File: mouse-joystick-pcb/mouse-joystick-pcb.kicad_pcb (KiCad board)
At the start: 4 copper layers, 60 x 160 mm, 77 parts, among them J1001 FFC_P1mm_BOT_RA_SMD, J1101 FFC_P1mm_BOT_RA_SMD, J501 FFC_P1mm_BOT_RA_SMD, J601 FFC_P1mm_BOT_RA_SMD, J701 FFC_P1mm_BOT_RA_SMD, J801 FFC_P1mm_BOT_RA_SMD, J901 FFC_P1mm_BOT_RA_SMD, Q301 MOSFET-N-CH-EN_100V_260mA, Q302 MOSFET-P-CH-EN_60V_50A, T301 TERM_BLK_HDR_2POS_90DEG_0.2IN, U1001 MAX13431E, U1101 MAX13431E, U301 TPSM365R6V5RDNR, U501 MAX13431E, U601 MAX13431E, U701 MAX13431E, U801 MAX13431E, U901 MAX13431E

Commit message: Adjust schmatic
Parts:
- removed A401: PICO_W5500_EVB, Janelia:Pico-W5500-EVB_Header_Holes
- removed C1001, C1101, C302, C501, C601, C701, C801, C901: 0.1uF_100V, Janelia:C_0402_1005Metric
- removed C1002, C1102, C502, C602, C702, C802, C902: 1uF_35V, Janelia:C_0402_1005Metric
- removed C301: 3.3uF_50V, Janelia:C_1210_3225Metric
- removed C303, C304: 1uF_25V, Janelia:C_0402_1005Metric
- removed D1001, D1101, D501, D601, D701, D801, D901: D_Zener_47V_1W, Janelia:D_SMA
- removed D1002, D1102, D502, D602, D702, D802, D902: D, Janelia:D_SMB
- removed D301: D_50V_15A, Janelia:POWERDI5_DIO
- removed D401: D_SCHOTTKY_20V_1A, Janelia:DIOM3616X98N
- removed FID201, FID202, FID203, FID204: FIDUCIAL_0.5mm_MASK1mm, Janelia:FIDUCIAL_0.5mm_Mask1mm
- removed H201, H202, H203, H204: MountingHole_M3_Pad, Janelia:MountingHole_3.2mm_M3_Pad
- removed J1001, J1101, J501, J601, J701, J801, J901: FFC_P1mm_BOT_RA_SMD, Janelia:CONN_C2914097
- removed Q301: MOSFET-N-CH-EN_100V_260mA, Janelia:SOT-23
- removed Q302: MOSFET-P-CH-EN_60V_50A, Janelia:TO-252-2
- removed R1001, R1101, R501, R601, R701, R801, R901: 0.24, Janelia:R_2512_6332Metric
- removed R1002, R1102, R502, R602, R702, R802, R902: 100, Janelia:R_0402_1005Metric
- removed R301: 1k, Janelia:R_0402_1005Metric
- removed R302: 3.6k, Janelia:R_0402_1005Metric
- removed T301: TERM_BLK_HDR_2POS_90DEG_0.2IN, Janelia:PHOENIX_1757242
- removed U1001, U1101, U501, U601, U701, U801, U901: MAX13431E, Janelia:21-0137I_T1033-1_MXM
- removed U301: TPSM365R6V5RDNR, Janelia:RDN0011A-MFG
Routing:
- net /GND: track 631.7 -> 0.00 mm, vias 31 -> 0
- net /+5V: track 263.8 -> 0.00 mm, vias 9 -> 0
- net /+3.3V: track 186.5 -> 0.00 mm, vias 7 -> 0
- net /VCC: track 160.5 -> 0.00 mm
- net /RX: track 150.3 -> 0.00 mm, vias 7 -> 0
- net /TX: track 147.8 -> 0.00 mm, vias 7 -> 0
- net /ENABLE_TX_6: track 77.9 -> 0.00 mm, vias 1 -> 0
- net /~{ENABLE_RX_6}: track 76.8 -> 0.00 mm, vias 1 -> 0
- net /power/VBB: track 66.0 -> 0.00 mm
- net /ENABLE_TX_5: track 62.2 -> 0.00 mm, vias 1 -> 0
- net /~{ENABLE_RX_5}: track 61.3 -> 0.00 mm, vias 1 -> 0
- net /ENABLE_TX_4: track 55.1 -> 0.00 mm, vias 1 -> 0
- net /power/~{ENABLE_VCC}: track 55.0 -> 0.00 mm, vias 2 -> 0
- net /~{ENABLE_RX_4}: track 54.5 -> 0.00 mm, vias 1 -> 0
- net /ENABLE_TX_3: track 38.4 -> 0.00 mm, vias 1 -> 0
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- removed copper zone on B.Cu, net /GND
- removed copper zone on In1.Cu, net /GND
- removed copper zone on In2.Cu, net /GND
- removed copper zone on F.Cu, net /VCC
- removed copper zone on F.Cu, net /power/VAA
- removed copper zone on F.Cu, net /power/VBB

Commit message: Initial pcb import
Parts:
- added A401: TEENSY_4.0_HEADERS, Janelia:TEENSY_4.0_HEADERS, F.Cu at (92.4, 39.7)
- added C301: 3.3uF_50V, Janelia:C_1210_3225Metric, F.Cu at (157.4, 39.2)
- added C302: 0.1uF_100V, Janelia:C_0402_1005Metric, F.Cu at (153.1, 38.1)
- added C303: 1uF_25V, Janelia:C_0402_1005Metric, F.Cu at (153.1, 40.1)
- added C304: 1uF_25V, Janelia:C_0402_1005Metric, F.Cu at (153.1, 42.0)
- added C305: 47uF_10V, Janelia:C_0805_2012Metric, F.Cu at (162.4, 38.6)
- added C501: 0.1uF_100V, Janelia:C_0402_1005Metric, F.Cu at (-57.2, 40.2)
- added C502: 0.1uF_100V, Janelia:C_0402_1005Metric, F.Cu at (-57.2, 42.1)
- added C503: 22nF_100V, Janelia:C_0603_1608Metric, F.Cu at (-86.0, 60.1)
- added C504: 0.1uF_100V, Janelia:C_0402_1005Metric, F.Cu at (-57.2, 44.1)
- added C505: 0.1uF_100V, Janelia:C_0402_1005Metric, F.Cu at (-57.2, 46.1)
- added C506: 0.47uF_35V, Janelia:C_0402_1005Metric, F.Cu at (-57.2, 48.0)
- added C507: 47uF_10V, Janelia:C_0805_2012Metric, F.Cu at (-54.7, 28.5)
- added C508: 0.1uF_100V, Janelia:C_0402_1005Metric, F.Cu at (-54.3, 40.2)
- added C509: 0.1uF_100V, Janelia:C_0402_1005Metric, F.Cu at (-54.3, 42.1)
- added C510: 0.1uF_100V, Janelia:C_0402_1005Metric, F.Cu at (-54.3, 44.1)
- added C511: 0.1uF_100V, Janelia:C_0402_1005Metric, F.Cu at (-54.3, 46.1)
- added C512: 2.2uF_100V, Janelia:C_0805_2012Metric, F.Cu at (-54.7, 31.5)
- added C513: 2.2uF_100V, Janelia:C_0805_2012Metric, F.Cu at (-54.7, 34.5)
- added C514: 100uF_50V, Janelia:CAP_EEEHAH101UAP, F.Cu at (-81.7, 44.1)
- added C515: 100uF_50V, Janelia:CAP_EEEHAH101UAP, F.Cu at (-81.7, 54.0)
- added C516: 0.1uF_100V, Janelia:C_0402_1005Metric, F.Cu at (-54.3, 48.0)
- added C517: 2.2uF_100V, Janelia:C_0805_2012Metric, F.Cu at (-54.7, 37.5)
- added C601: 0.22uF_25V, Janelia:C_0402_1005Metric, F.Cu at (-50.4, 88.5)
- added C602: 0.22uF_25V, Janelia:C_0402_1005Metric, F.Cu at (-50.4, 90.5)
- added C603: 1uF_35V, Janelia:C_0402_1005Metric, F.Cu at (-50.4, 92.5)
- added C604: 0.22uF_25V, Janelia:C_0402_1005Metric, F.Cu at (-50.4, 94.4)
- added C701: 0.1uF_100V, Janelia:C_0402_1005Metric, F.Cu at (-36.4, 39.6)
- added C702: 0.1uF_100V, Janelia:C_0402_1005Metric, F.Cu at (-36.4, 41.6)
- added C703: 22nF_100V, Janelia:C_0603_1608Metric, F.Cu at (-22.4, 55.6)
- added C704: 0.1uF_100V, Janelia:C_0402_1005Metric, F.Cu at (-36.4, 43.5)
- added C705: 0.1uF_100V, Janelia:C_0402_1005Metric, F.Cu at (-36.4, 45.5)
- added C706: 0.47uF_35V, Janelia:C_0402_1005Metric, F.Cu at (-36.4, 47.5)
- added C707: 47uF_10V, Janelia:C_0805_2012Metric, F.Cu at (-22.6, 40.1)
- added C708: 0.1uF_100V, Janelia:C_0402_1005Metric, F.Cu at (-36.4, 49.4)
- added C709: 0.1uF_100V, Janelia:C_0402_1005Metric, F.Cu at (-36.4, 51.4)
- added C710: 2.2uF_100V, Janelia:C_0805_2012Metric, F.Cu at (-22.6, 43.1)
- added C711: 2.2uF_100V, Janelia:C_0805_2012Metric, F.Cu at (-22.6, 46.1)
- added C712: 100uF_50V, Janelia:CAP_EEEHAH101UAP, F.Cu at (-44.1, 31.9)
- added C713: 100uF_50V, Janelia:CAP_EEEHAH101UAP, F.Cu at (-44.1, 41.8)
- added C801: 100uF_50V, Janelia:CAP_EEEHAH101UAP, F.Cu at (-23.3, 69.1)
- added D301: D_50V_15A, Janelia:POWERDI5_DIO, F.Cu at (112.4, 44.1)
- added D302: LED_RED, Janelia:LED_0402-1005_KNB, F.Cu at (142.4, 24.1)
- added FID201: FIDUCIAL_0.5mm_MASK1mm, Janelia:FIDUCIAL_0.5mm_Mask1mm, F.Cu at (74.9, 31.6)
- added FID202: FIDUCIAL_0.5mm_MASK1mm, Janelia:FIDUCIAL_0.5mm_Mask1mm, F.Cu at (129.9, 31.6)
- added FID203: FIDUCIAL_0.5mm_MASK1mm, Janelia:FIDUCIAL_0.5mm_Mask1mm, F.Cu at (129.9, 171.6)
- added FID204: FIDUCIAL_0.5mm_MASK1mm, Janelia:FIDUCIAL_0.5mm_Mask1mm, F.Cu at (74.9, 171.6)
- added H201: MountingHole_M3_Pad, Janelia:MountingHole_3.2mm_M3_Pad, F.Cu at (77.4, 26.6)
- added H202: MountingHole_M3_Pad, Janelia:MountingHole_3.2mm_M3_Pad, F.Cu at (127.4, 26.6)
- added H203: MountingHole_M3_Pad, Janelia:MountingHole_3.2mm_M3_Pad, F.Cu at (127.4, 176.6)
- added H204: MountingHole_M3_Pad, Janelia:MountingHole_3.2mm_M3_Pad, F.Cu at (77.4, 176.6)
- added J301: 2.1, Janelia:Connector_BarrelJack_XKB_2.1, F.Cu at (112.4, 29.1)
- added J501: Conn_01x02_P3.5mm_TBH_Horizontal_Screw, Janelia:PhoenixContact_MC_1,5_2-G-3.5_1x02_P3.50mm_Horizontal_Screw, F.Cu at (-61.9, 30.2)
- added J502: Conn_01x04_P3.5mm_TBH_Horizontal_Screw, Janelia:PhoenixContact_MC_1,5_4-G-3.5_1x04_P3.50mm_Horizontal_Screw, F.Cu at (-67.0, 42.2)
- added J503: Conn_01x05_P3.5mm_TBH_Horizontal_Screw, Janelia:PhoenixContact_MC_1,5_5-G-3.5_1x05_P3.50mm_Horizontal_Screw, F.Cu at (-77.4, 30.2)
- added J701: Conn_01x02_P3.5mm_TBH_Horizontal_Screw, Janelia:PhoenixContact_MC_1,5_2-G-3.5_1x02_P3.50mm_Horizontal_Screw, F.Cu at (-29.9, 41.8)
- added J702: Conn_01x04_P3.5mm_TBH_Horizontal_Screw, Janelia:PhoenixContact_MC_1,5_4-G-3.5_1x04_P3.50mm_Horizontal_Screw, F.Cu at (-29.4, 30.1)
- added J801: Conn_01x02_P3.5mm_TBH_Horizontal_Screw, Janelia:PhoenixContact_MC_1,5_2-G-3.5_1x02_P3.50mm_Horizontal_Screw, F.Cu at (-24.6, 77.1)
- added R301: 2.32k, Janelia:R_0805_2012Metric, F.Cu at (138.3, 27.7)
- added R501: 0.36, Janelia:R_1206_3216Metric, F.Cu at (-61.2, 52.4)
- added R502: 0.36, Janelia:R_1206_3216Metric, F.Cu at (-61.2, 55.7)
- added R503: 10, Janelia:R_0402_1005Metric, F.Cu at (-56.9, 58.8)
- added R504: 200k, Janelia:R_0402_1005Metric, F.Cu at (-56.9, 60.8)
- added R601: 40k, Janelia:R_0603_1608Metric, F.Cu at (-49.8, 96.7)
- added R602: 40k, Janelia:R_0603_1608Metric, F.Cu at (-49.8, 99.2)
- added R701: 0.12, Janelia:R_1206_3216Metric, F.Cu at (-32.1, 52.2)
- added R702: 0.12, Janelia:R_1206_3216Metric, F.Cu at (-32.1, 55.5)
- added R703: 10, Janelia:R_0402_1005Metric, F.Cu at (-27.9, 56.1)
- added R801: 30, Janelia:R_0402_1005Metric, F.Cu at (-18.1, 79.4)
- added SP601: Speaker_13x13mm_8Ohm_700mW, Janelia:Speaker_13x13mm_KLJ-01304T-08R07W, F.Cu at (-59.3, 94.8)
- added U301: TPSM365R6V5RDNR, Janelia:RDN0011A-MFG, F.Cu at (149.0, 40.5)
- added U501: MAX6816, Janelia:SOT192P237X122-4N, F.Cu at (-61.5, 59.7)
- added U502: TMC5130A-TA, Janelia:TQFP-48-1EP_7x7mm_P0.5mm_EP5x5mm_ThermalVias, F.Cu at (-69.7, 56.5)
- added U503: Logic_LevelTranslator_LSF0102DCUR, Janelia:SOP50P310X90-8N, F.Cu at (-55.1, 52.4)
- added U601: TPA6204A1DRBR, Janelia:DRB8_1P75X1P5, F.Cu at (-63.8, 104.4)
- added U701: MAX6816, Janelia:SOT192P237X122-4N, F.Cu at (-26.9, 52.8)
- added U702: TMC5130A-TA, Janelia:TQFP-48-1EP_7x7mm_P0.5mm_EP5x5mm_ThermalVias, F.Cu at (-44.8, 52.4)
- added U801: 40V_200mA, Janelia:SC-74-6_1.55x2.9mm_P0.95mm, F.Cu at (-16.2, 76.2)
- added X501: 16MHz_3.3V, Janelia:OSC_ECS-2520S33-160-FN-TR, F.Cu at (-55.8, 55.9)
- added X701: 16MHz_3.3V, Janelia:OSC_ECS-2520S33-160-FN-TR, F.Cu at (-21.8, 52.4)
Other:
- board text added: "+24VDC Center Positive"
- board text added: "mouse-joystick-pcb v1.0 2024/10"
- board text removed: "+48VDC"
- board text removed: "0"
- board text removed: "1"
- board text removed: "2"
- board text removed: "3"
- board text removed: "4"
- board text removed: "5"
- board text removed: "6"
- board text removed: "GND"
- board text removed: "RX"
- board text removed: "TX"
- board text removed: "mouse-joystick-pcb v1.0 2024/07"

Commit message: Initial footprint layout
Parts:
- moved J503 210.1 mm to (124.4, 88.6), turned to 90 degrees
- moved C503 200.6 mm to (114.4, 70.1)
- moved C712 194.4 mm to (116.4, 141.6), turned to -90 degrees
- moved J502 193.5 mm to (124.4, 70.6), turned to 90 degrees
- moved C515 193.4 mm to (108.4, 89.6), turned to 180 degrees
- moved C701 190.9 mm to (122.4, 145.6), turned to 180 degrees
- moved C514 190.9 mm to (108.4, 61.6), turned to 180 degrees
- moved J501 188.3 mm to (124.4, 57.6), turned to 90 degrees
- moved J701 183.4 mm to (115.4, 153.6)
- moved C517 181.3 mm to (120.4, 84.6), turned to 90 degrees
- moved J702 180.7 mm to (102.4, 153.6)
- moved U502 180.1 mm to (109.4, 75.6)
- moved U501 180.0 mm to (118.4, 57.6), turned to 180 degrees
- moved C516 179.4 mm to (120.4, 88.6), turned to -90 degrees
- moved C511 177.6 mm to (117.4, 91.6)
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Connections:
- A401 pad 10: unconnected-(A401-D10/CS/MQSR/PWM-Pad10) -> /BRAKE_PWM
- A401 pad 22: /BRAKE_PWM -> unconnected-(A401-D22/A8/CTX1/PWM-Pad22)
- A401 pad 23: /AUDIO -> unconnected-(A401-D23/A9/CRX1/MCLK1/PWM-Pad23)
- A401 pad 9: unconnected-(A401-D9/OUT1C/PWM-Pad9) -> /AUDIO
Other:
- board size 60 x 160 mm -> 60 x 120 mm

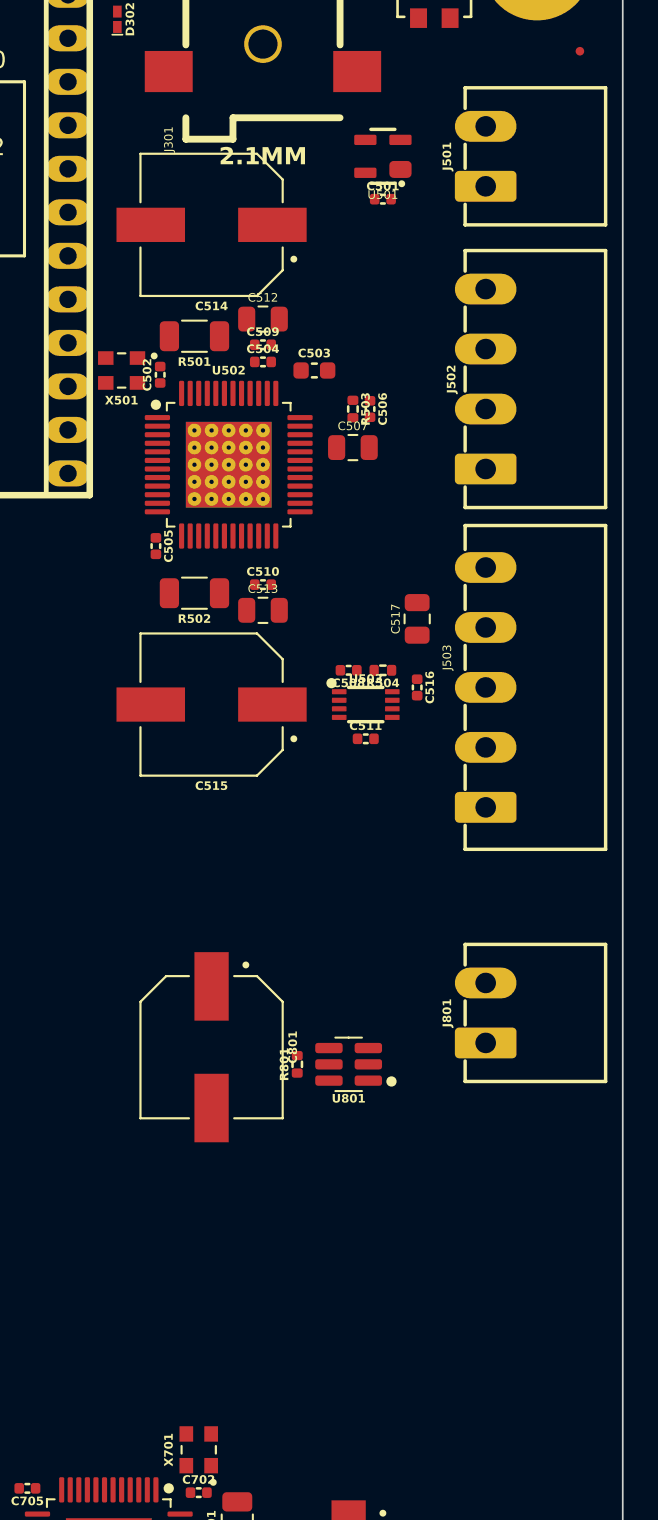
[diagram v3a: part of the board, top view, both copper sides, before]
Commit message: Add torque-sensor sheet
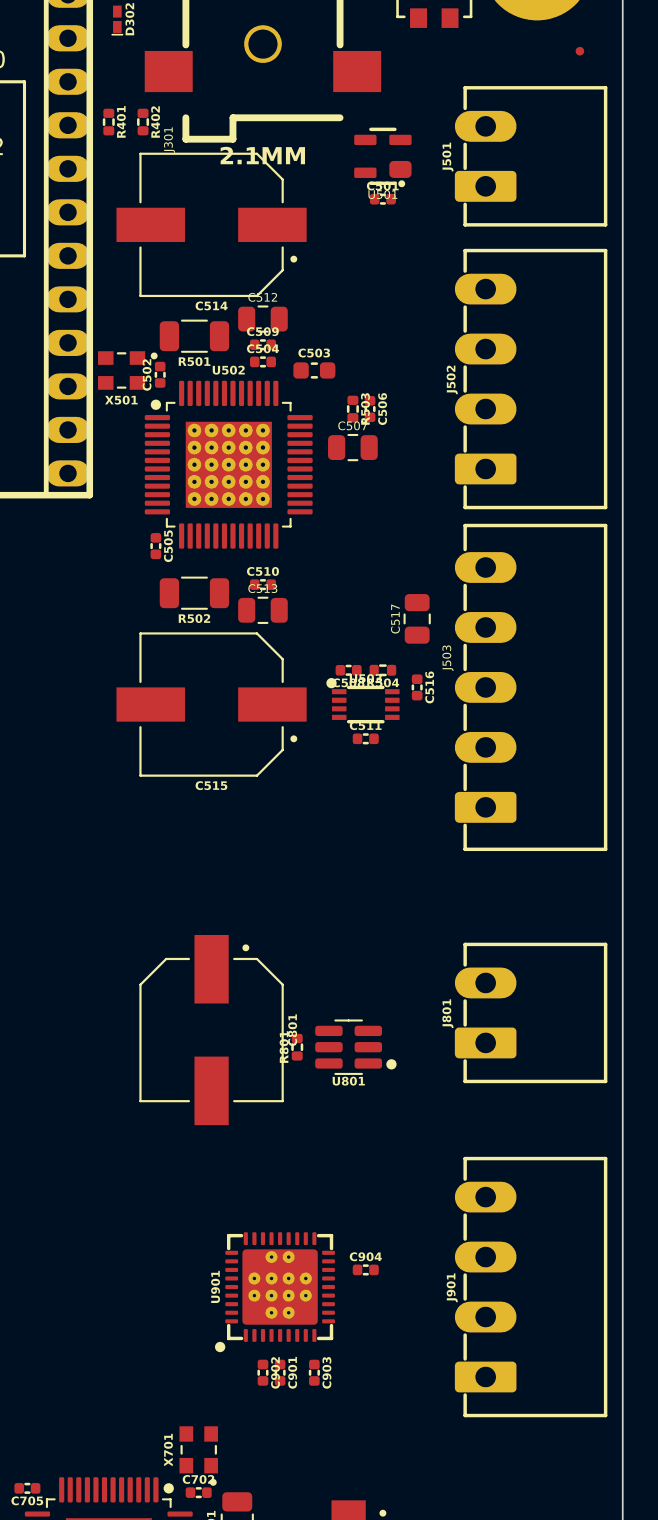
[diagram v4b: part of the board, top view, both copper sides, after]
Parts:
- added C901: 0.1uF_100V, Janelia:C_0402_1005Metric, F.Cu at (112.4, 128.6)
- added C902: 0.1uF_100V, Janelia:C_0402_1005Metric, F.Cu at (111.4, 128.6)
- added C903: 0.1uF_100V, Janelia:C_0402_1005Metric, F.Cu at (114.4, 128.6)
- added C904: 0.1uF_100V, Janelia:C_0402_1005Metric, F.Cu at (117.4, 122.6)
- added J901: Conn_01x04_P3.5mm_TBH_Horizontal_Screw, Janelia:PhoenixContact_MC_1,5_4-G-3.5_1x04_P3.50mm_Horizontal_Screw, F.Cu at (124.4, 123.6)
- added R401: 1.8k, Janelia:R_0402_1005Metric, F.Cu at (102.4, 55.6)
- added R402: 1.8k, Janelia:R_0402_1005Metric, F.Cu at (104.4, 55.6)
- added U901: PGA305ARHHR, Janelia:RHH0036C, F.Cu at (112.4, 123.6)
- moved C801 1.00 mm to (108.4, 108.6)
- moved R801 1.00 mm to (113.4, 109.6)
- moved U801 1.00 mm to (116.4, 109.6)
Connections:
- A401 pad 18: /~{MOTOR_CS_1} -> /SDA
- A401 pad 19: /MOTOR_DIAG0_1 -> /SCL
- A401 pad 7: unconnected-(A401-D7/RX2/OUT1A/PWM-Pad7) -> /MOTOR_DIAG0_1
- A401 pad 8: unconnected-(A401-D8/TX2/IN1/PWM-Pad8) -> /~{MOTOR_CS_1}
